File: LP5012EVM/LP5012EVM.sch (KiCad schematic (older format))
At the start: 10 parts, among them J1 Main Connector, U1 LP5012

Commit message: Inclusion de PCB
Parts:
- removed D3, D4: LED_RGB, LED_SMD:LED_RGB_5050-6, symbol Device:LED_RGB
- added D1, D2, D3, D4, D5, D6: LED, LED_SMD:LED_0805_2012Metric, symbol Device:LED
- D7: renamed from D1; footprint LED_SMD:LED_RGB_5050-6 -> LED_SMD:LED_RGB_1210; symbol Device:LED_RGB -> Device:LED_ABRG
- D8: renamed from D2; footprint LED_SMD:LED_RGB_5050-6 -> LED_SMD:LED_RGB_1210; symbol Device:LED_RGB -> Device:LED_ABRG
- U1: footprint (none) -> Footprint LP5012:PQFN21P40_300X300X80L40X20T180
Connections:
- net LB0: now also D1.1 (K); no longer D7.1 (RK)
- net LB1: now also D2.1 (K); no longer D7.2 (GK)
- net LB10: now also D8.4 (GK)
- net LB11: now also D8.2 (BK)
- net LB2: now also D3.1 (K); no longer D7.3 (BK)
- net LB3: now also D4.1 (K); no longer D8.1 (RK)
- net LB4: now also D5.1 (K); no longer D8.2 (GK)
- net LB5: now also D6.1 (K); no longer D8.3 (BK)
- net LB6: now also D7.3 (RK)
- net LB7: now also D7.4 (GK)
- net LB8: now also D7.2 (BK)
- net LB9: now also D8.3 (RK)
- net VCC: now also D7.1 (A), D8.1 (A), D1.2 (A), D2.2 (A), D3.2 (A), D4.2 (A), D5.2 (A), D6.2 (A); no longer D7.4 (BA), D7.5 (GA), D7.6 (RA), D8.4 (BA), D8.5 (GA), D8.6 (RA)
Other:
- note added: "LEDs"
- note removed: "RGB LEDs"
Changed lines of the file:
@@
 EESchema Schematic File Version 4
-LIBS:LP5012EVM_Custom-cache
+LIBS:LP5012EVM-cache
 EELAYER 30 0
 EELAYER END
@@
 $EndComp
 $Comp
-L Device:LED_RGB D1
+L Device:LED_ABRG D7
 U 1 1 5D929F43
-P 9400 2300
-F 0 "D1" H 9400 2797 50  0000 C CNN
-F 1 "LED_RGB" H 9400 2706 50  0000 C CNN
-F 2 "LED_SMD:LED_RGB_5050-6" H 9400 2250 50  0001 C CNN
-F 3 "~" H 9400 2250 50  0001 C CNN
-	1    9400 2300
-	1    0    0    -1
-$EndComp
-$Comp
-L Device:LED_RGB D2
-U 1 1 5D92CB70
-P 9400 3250
-F 0 "D2" H 9400 3747 50  0000 C CNN
-F 1 "LED_RGB" H 9400 3656 50  0000 C CNN
-F 2 "LED_SMD:LED_RGB_5050-6" H 9400 3200 50  0001 C CNN
-F 3 "~" H 9400 3200 50  0001 C CNN
-	1    9400 3250
-	1    0    0    -1
-$EndComp
-$Comp
-L Device:LED_RGB D3
-U 1 1 5D92D562
 P 9400 4350
-F 0 "D3" H 9400 4847 50  0000 C CNN
-F 1 "LED_RGB" H 9400 4756 50  0000 C CNN
-F 2 "LED_SMD:LED_RGB_5050-6" H 9400 4300 50  0001 C CNN
+F 0 "D7" H 9350 4750 50  0000 C CNN
+F 1 "LED_RGB" H 9400 4000 50  0001 C CNN
+F 2 "LED_SMD:LED_RGB_1210" H 9400 4300 50  0001 C CNN
 F 3 "~" H 9400 4300 50  0001 C CNN
 	1    9400 4350
@@
 $EndComp
 $Comp
-L Device:LED_RGB D4
-U 1 1 5D92EA6C
+L Device:LED_ABRG D8
+U 1 1 5D92CB70
 P 9400 5300
-F 0 "D4" H 9400 5797 50  0000 C CNN
-F 1 "LED_RGB" H 9400 5706 50  0000 C CNN
-F 2 "LED_SMD:LED_RGB_5050-6" H 9400 5250 50  0001 C CNN
+F 0 "D8" H 9350 5700 50  0000 C CNN
+F 1 "LED_RGB" H 9400 4950 50  0001 C CNN
+F 2 "LED_SMD:LED_RGB_1210" H 9400 5250 50  0001 C CNN
 F 3 "~" H 9400 5250 50  0001 C CNN
 	1    9400 5300
@@
 LB9
 Wire Wire Line
-	9200 2100 9050 2100
-Wire Wire Line
-	9200 2300 9050 2300
-Wire Wire Line
-	9200 2500 9050 2500
-Wire Wire Line
-	9050 3050 9200 3050
-Wire Wire Line
-	9200 3250 9050 3250
-Wire Wire Line
-	9050 3450 9200 3450
-Wire Wire Line
 	9200 4150 9050 4150
 Wire Wire Line
-	9050 4350 9200 4350
+	9200 4350 9050 4350
 Wire Wire Line
 	9200 4550 9050 4550
 Wire Wire Line
 	9050 5100 9200 5100
+Wire Wire Line
+	9200 5300 9050 5300
 Wire Wire Line
 	9050 5500 9200 5500
 Text Label 9050 5500 2    50   ~ 0
 LB11
-Wire Wire Line
-	9200 5300 9050 5300
 Text Label 9050 5300 2    50   ~ 0
 LB10
@@
 F 0 "U1" H 6000 3950 50  0000 C CNN
 F 1 "LP5012" H 6150 2050 50  0000 C CNN
-F 2 "" H 6250 3950 50  0001 C CNN
+F 2 "Footprint LP5012:PQFN21P40_300X300X80L40X20T180" H 6250 3950 50  0001 C CNN
 F 3 "" H 6250 3950 50  0000 C CNN
 	1    6300 3300
@@
 P 1950 3600
 F 0 "J1" H 2030 3642 50  0000 L CNN
-F 1 "Main Connector" H 2030 3551 50  0000 L CNN
+F 1 "Main Connector" H 2030 3551 50  0001 L CNN
 F 2 "Connector_PinHeader_2.54mm:PinHeader_1x07_P2.54mm_Vertical" H 1950 3600 50  0001 C CNN
 F 3 "~" H 1950 3600 50  0001 C CNN
@@
 Text Label 1350 3700 0    50   ~ 0
 IN_EN
-Text Label 1350 3500 0    50   ~ 0
-SCL
-Text Label 1350 3600 0    50   ~ 0
-SDA
 Text Label 1350 3800 0    50   ~ 0
 ADDR0
@@
 L power:VCC #PWR0107
 U 1 1 5D98000B
+P 9900 4000
+F 0 "#PWR0107" H 9900 3850 50  0001 C CNN
+F 1 "VCC" H 9917 4173 50  0000 C CNN
+F 2 "" H 9900 4000 50  0001 C CNN
+F 3 "" H 9900 4000 50  0001 C CNN
+	1    9900 4000
+	1    0    0    -1
+$EndComp
+$Comp
+L power:VCC #PWR0110
+U 1 1 5D981315
+P 9900 4950
+F 0 "#PWR0110" H 9900 4800 50  0001 C CNN
+F 1 "VCC" H 9917 5123 50  0000 C CNN
+F 2 "" H 9900 4950 50  0001 C CNN
+F 3 "" H 9900 4950 50  0001 C CNN
+	1    9900 4950
+	1    0    0    -1
+$EndComp
+$Comp
+L power:VCC #PWR0111
+U 1 1 5D981A4D
 P 9900 1950
-F 0 "#PWR0107" H 9900 1800 50  0001 C CNN
+F 0 "#PWR0111" H 9900 1800 50  0001 C CNN
 F 1 "VCC" H 9917 2123 50  0000 C CNN
 F 2 "" H 9900 1950 50  0001 C CNN
@@
 $EndComp
 $Comp
-L power:VCC #PWR0110
-U 1 1 5D981315
-P 9900 2900
-F 0 "#PWR0110" H 9900 2750 50  0001 C CNN
-F 1 "VCC" H 9917 3073 50  0000 C CNN
-F 2 "" H 9900 2900 50  0001 C CNN
-F 3 "" H 9900 2900 50  0001 C CNN
-	1    9900 2900
-	1    0    0    -1
-$EndComp
-$Comp
-L power:VCC #PWR0111
-U 1 1 5D981A4D
-P 9900 4000
-F 0 "#PWR0111" H 9900 3850 50  0001 C CNN
-F 1 "VCC" H 9917 4173 50  0000 C CNN
-F 2 "" H 9900 4000 50  0001 C CNN
-F 3 "" H 9900 4000 50  0001 C CNN
-	1    9900 4000
-	1    0    0    -1
-$EndComp
-$Comp
 L power:VCC #PWR0112
 U 1 1 5D981FA3
-P 9950 4950
-F 0 "#PWR0112" H 9950 4800 50  0001 C CNN
-F 1 "VCC" H 9967 5123 50  0000 C CNN
-F 2 "" H 9950 4950 50  0001 C CNN
-F 3 "" H 9950 4950 50  0001 C CNN
-	1    9950 4950
-	1    0    0    -1
-$EndComp
+P 9950 2900
+F 0 "#PWR0112" H 9950 2750 50  0001 C CNN
+F 1 "VCC" H 9967 3073 50  0000 C CNN
+F 2 "" H 9950 2900 50  0001 C CNN
+F 3 "" H 9950 2900 50  0001 C CNN
+	1    9950 2900
+	1    0    0    -1
+$EndComp
+Wire Wire Line
+	9600 5300 9900 5300
 Wire Wire Line
 	9900 2500 9900 2300
-Wire Wire Line
-	9600 2500 9900 2500
 Connection ~ 9900 2100
 Wire Wire Line
 	9900 2100 9900 1950
-Wire Wire Line
-	9600 2100 9900 2100
 Connection ~ 9900 2300
 Wire Wire Line
 	9900 2300 9900 2100
 Wire Wire Line
-	9900 3450 9900 3250
-Wire Wire Line
-	9600 3450 9900 3450
-Wire Wire Line
-	9600 3050 9900 3050
-Connection ~ 9900 3050
-Wire Wire Line
-	9900 3050 9900 2900
-Wire Wire Line
-	9600 3250 9900 3250
-Connection ~ 9900 3250
-Wire Wire Line
-	9900 3250 9900 3050
-Wire Wire Line
-	9900 4550 9900 4350
-Wire Wire Line
-	9600 4550 9900 4550
-Wire Wire Line
-	9600 4150 9900 4150
-Connection ~ 9900 4150
-Wire Wire Line
-	9900 4150 9900 4000
+	9950 3450 9950 3250
+Connection ~ 9950 3050
+Wire Wire Line
+	9950 3050 9950 2900
+Connection ~ 9950 3250
+Wire Wire Line
+	9950 3250 9950 3050
 Wire Wire Line
 	9600 4350 9900 4350
-Connection ~ 9900 4350
-Wire Wire Line
-	9900 4350 9900 4150
-Wire Wire Line
-	9950 5500 9950 5300
-Wire Wire Line
-	9600 5500 9950 5500
-Wire Wire Line
-	9600 5100 9950 5100
-Connection ~ 9950 5100
-Wire Wire Line
-	9950 5100 9950 4950
-Wire Wire Line
-	9600 5300 9950 5300
-Connection ~ 9950 5300
-Wire Wire Line
-	9950 5300 9950 5100
-Wire Wire Line
-	9600 2300 9900 2300
 Wire Notes Line
 	950  2400 3400 2400
@@
 Wire Notes Line
 	8650 5850 8650 1500
-Text Notes 1000 5050 0    50   ~ 0
+Text Notes 1000 5100 0    79   ~ 0
 Header to interface with the host side
-Text Notes 3950 5200 0    50   ~ 0
+Text Notes 3950 5250 0    98   ~ 0
 LED Driver IC
-Text Notes 8750 5950 0    50   ~ 0
-RGB LEDs
+Text Notes 8700 6000 0    98   ~ 0
+LEDs
 Text Notes 7000 6950 0    98   ~ 0
 Author: Jhonattan Camargo
+Text Label 1350 3600 0    50   ~ 0
+SDA
+Text Label 1350 3500 0    50   ~ 0
+SCL
+$Comp
+L Device:LED D1
+U 1 1 5D9A8567
+P 9400 2100
+F 0 "D1" H 9550 2200 50  0000 C CNN
+F 1 "LED" H 9393 2225 50  0001 C CNN
+F 2 "LED_SMD:LED_0805_2012Metric" H 9400 2100 50  0001 C CNN
+F 3 "~" H 9400 2100 50  0001 C CNN
+	1    9400 2100
+	1    0    0    -1
+$EndComp
+$Comp
+L Device:LED D2
+U 1 1 5D9A9184
+P 9400 2300
+F 0 "D2" H 9550 2400 50  0000 C CNN
+F 1 "LED" H 9393 2425 50  0001 C CNN
+F 2 "LED_SMD:LED_0805_2012Metric" H 9400 2300 50  0001 C CNN
+F 3 "~" H 9400 2300 50  0001 C CNN
+	1    9400 2300
+	1    0    0    -1
+$EndComp
+$Comp
+L Device:LED D3
+U 1 1 5D9A955B
+P 9400 2500
+F 0 "D3" H 9550 2600 50  0000 C CNN
+F 1 "LED" H 9393 2625 50  0001 C CNN
+F 2 "LED_SMD:LED_0805_2012Metric" H 9400 2500 50  0001 C CNN
+F 3 "~" H 9400 2500 50  0001 C CNN
+	1    9400 2500
+	1    0    0    -1
+$EndComp
+$Comp
+L Device:LED D4
+U 1 1 5D9A9A6A
+P 9400 3050
+F 0 "D4" H 9550 3150 50  0000 C CNN
+F 1 "LED" H 9393 3175 50  0001 C CNN
+F 2 "LED_SMD:LED_0805_2012Metric" H 9400 3050 50  0001 C CNN
+F 3 "~" H 9400 3050 50  0001 C CNN
+	1    9400 3050
+	1    0    0    -1
+$EndComp
+$Comp
+L Device:LED D5
+U 1 1 5D9AA001
+P 9400 3250
+F 0 "D5" H 9550 3350 50  0000 C CNN
+F 1 "LED" H 9393 3375 50  0001 C CNN
+F 2 "LED_SMD:LED_0805_2012Metric" H 9400 3250 50  0001 C CNN
+F 3 "~" H 9400 3250 50  0001 C CNN
+	1    9400 3250
+	1    0    0    -1
+$EndComp
+$Comp
+L Device:LED D6
+U 1 1 5D9AA1F8
+P 9400 3450
+F 0 "D6" H 9550 3550 50  0000 C CNN
+F 1 "LED" H 9393 3575 50  0001 C CNN
+F 2 "LED_SMD:LED_0805_2012Metric" H 9400 3450 50  0001 C CNN
+F 3 "~" H 9400 3450 50  0001 C CNN
+	1    9400 3450
+	1    0    0    -1
+$EndComp
+Wire Wire Line
+	9050 2100 9250 2100
+Wire Wire Line
+	9050 2300 9250 2300
+Wire Wire Line
+	9550 2100 9900 2100
+Wire Wire Line
+	9550 2300 9900 2300
+Wire Wire Line
+	9050 2500 9250 2500
+Wire Wire Line
+	9550 2500 9900 2500
+Wire Wire Line
+	9050 3050 9250 3050
+Wire Wire Line
+	9050 3250 9250 3250
+Wire Wire Line
+	9050 3450 9250 3450
+Wire Wire Line
+	9550 3450 9950 3450
+Wire Wire Line
+	9550 3250 9950 3250
+Wire Wire Line
+	9550 3050 9950 3050
+Wire Wire Line
+	9900 4950 9900 5300
+Wire Wire Line
+	9900 4000 9900 4350
 $EndSCHEMATC

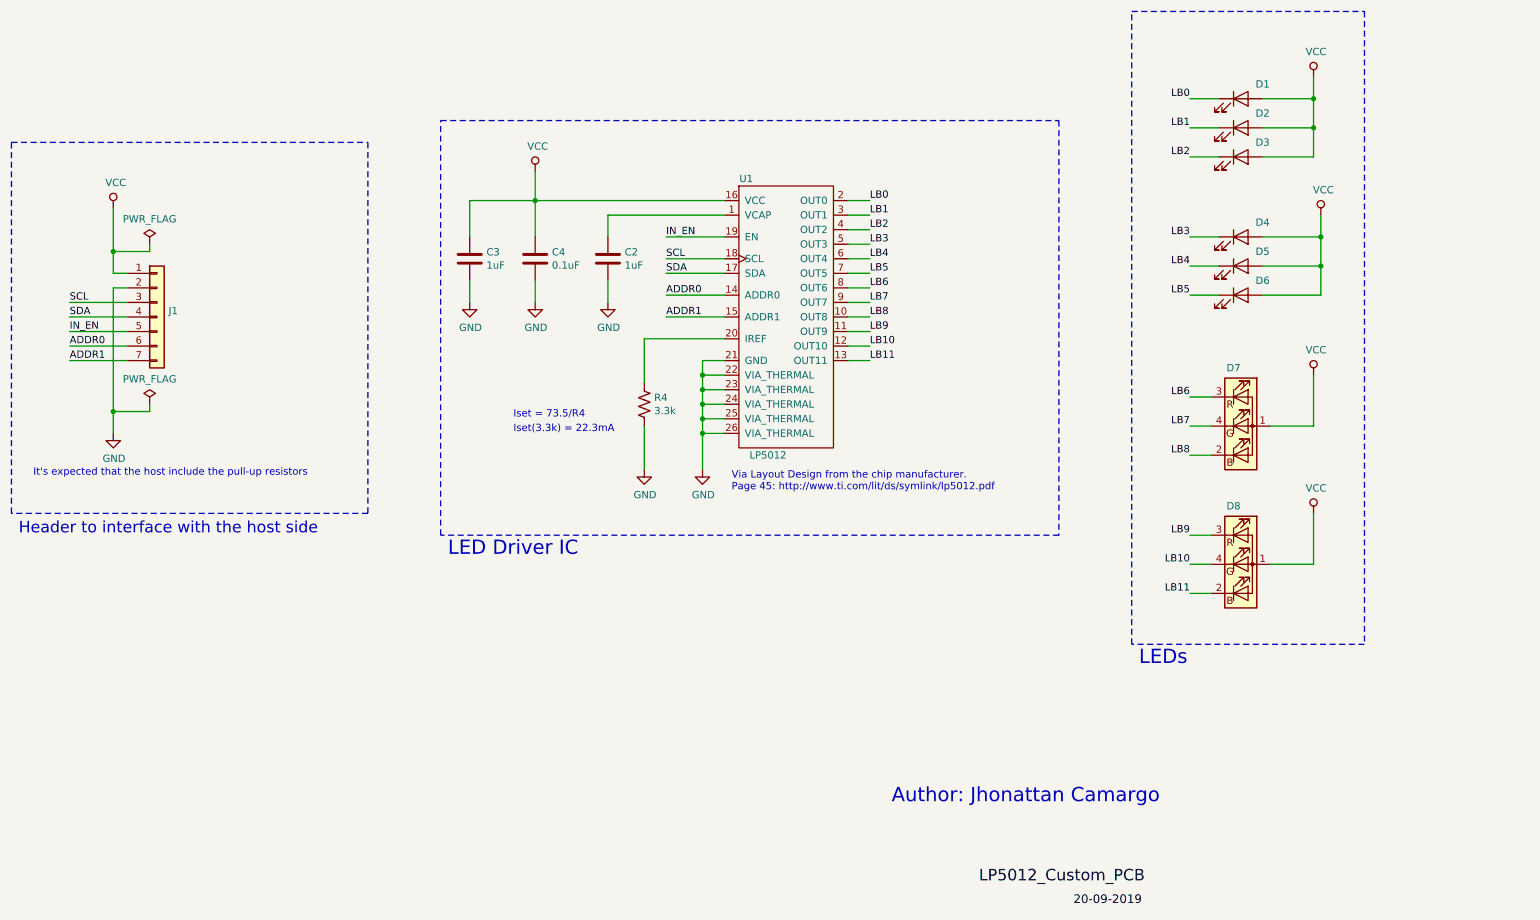
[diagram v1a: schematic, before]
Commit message: Inclusión de avance de PCB
Inclusión de planos, queda pendiente agregar modelos 3D de agunos componentes
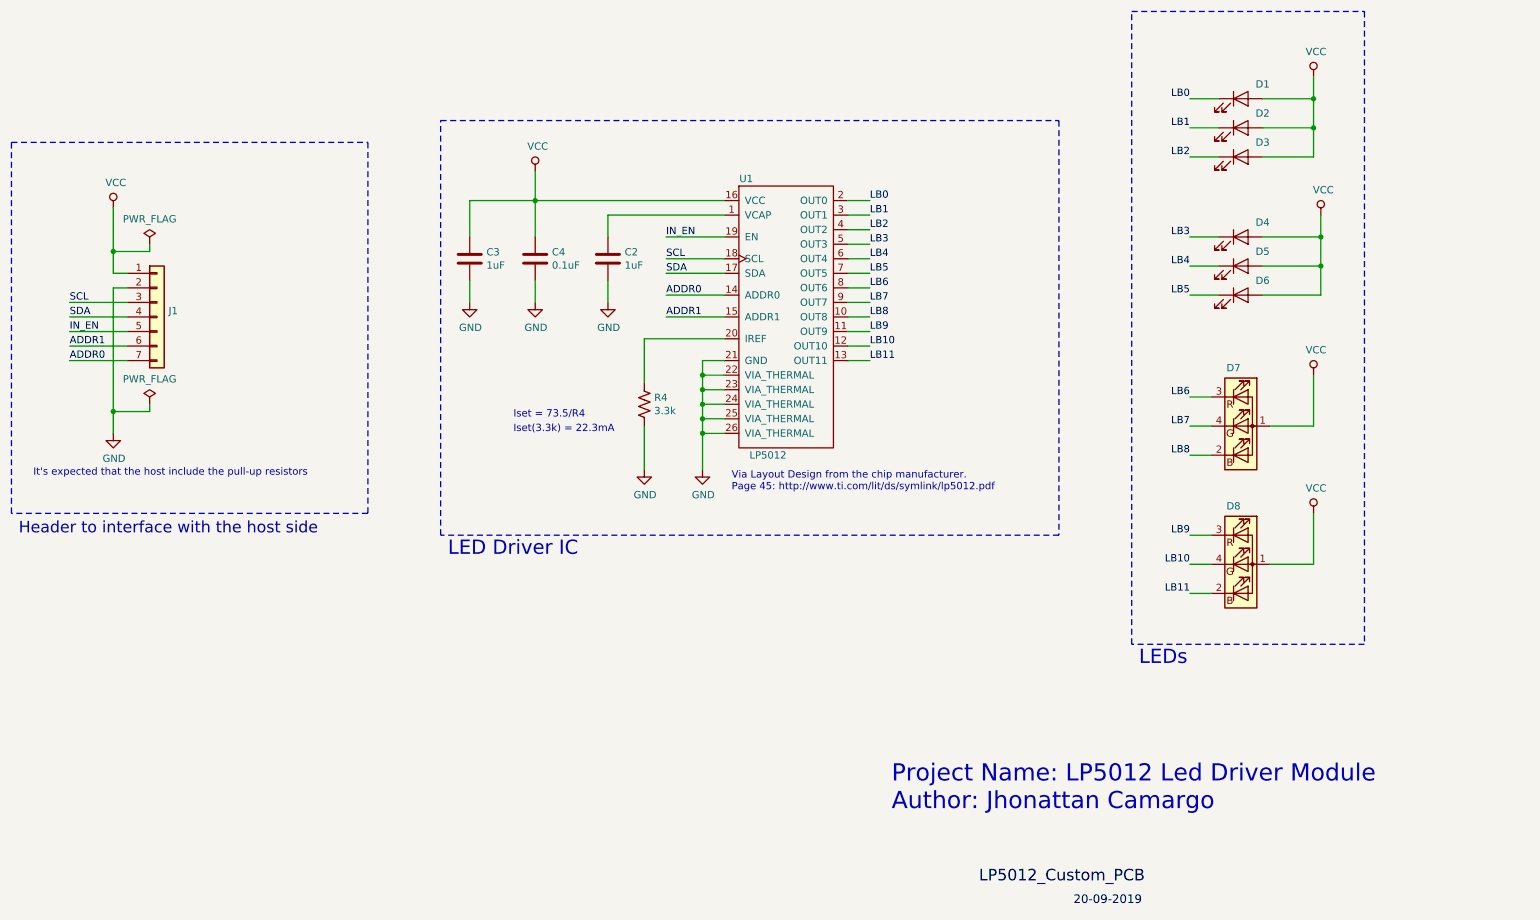
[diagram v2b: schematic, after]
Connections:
- net ADDR0: now also J1.7 (Pin_7); no longer J1.6 (Pin_6)
- net ADDR1: now also J1.6 (Pin_6); no longer J1.7 (Pin_7)
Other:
- note added: "Project Name: LP5012 Led Driver Module\nAuthor: Jhonattan Camargo"
- note removed: "Author: Jhonattan Camargo"
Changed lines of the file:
@@
 Text Label 1350 3700 0    50   ~ 0
 IN_EN
-Text Label 1350 3800 0    50   ~ 0
-ADDR0
-Text Label 1350 3900 0    50   ~ 0
-ADDR1
 Wire Wire Line
 	1650 2850 1650 3150
@@
 	1350 3700 1750 3700
 Wire Wire Line
-	1750 3800 1350 3800
-Wire Wire Line
 	1750 3900 1350 3900
 Wire Wire Line
@@
 Text Notes 8700 6000 0    98   ~ 0
 LEDs
-Text Notes 7000 6950 0    98   ~ 0
-Author: Jhonattan Camargo
 Text Label 1350 3600 0    50   ~ 0
 SDA
@@
 Wire Wire Line
 	9900 4000 9900 4350
+Text Notes 7000 7000 0    118  ~ 0
+Project Name: LP5012 Led Driver Module\nAuthor: Jhonattan Camargo
+Text Label 1350 3800 0    50   ~ 0
+ADDR1
+Wire Wire Line
+	1750 3800 1350 3800
+Text Label 1350 3900 0    50   ~ 0
+ADDR0
 $EndSCHEMATC

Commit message: Inclusión de algunos aspectos de la corrección del compañero
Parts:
- U1: footprint Footprint LP5012:PQFN21P40_300X300X80L40X20T180 -> Footprint LP5012:LP5012
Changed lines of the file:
@@
 F 0 "U1" H 6000 3950 50  0000 C CNN
 F 1 "LP5012" H 6150 2050 50  0000 C CNN
-F 2 "Footprint LP5012:PQFN21P40_300X300X80L40X20T180" H 6250 3950 50  0001 C CNN
+F 2 "Footprint LP5012:LP5012" H 6250 3950 50  0001 C CNN
 F 3 "" H 6250 3950 50  0000 C CNN
 	1    6300 3300
